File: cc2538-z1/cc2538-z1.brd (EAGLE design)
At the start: 56.8 x 34.5 mm, 101 parts, among them U1 CC2538, U10 DMG6602SVT, U2 CC1120_RHM_32, U3 TPD2E001IDRLRQ1, U4 CP2103, U5 BSS138PS, U6 BSS138PS, U7 BSS138PS, U8 M25P16VMN6P, U9 DMG6602SVT, X1 FA-128, X2 32MHz, X3 32.768K

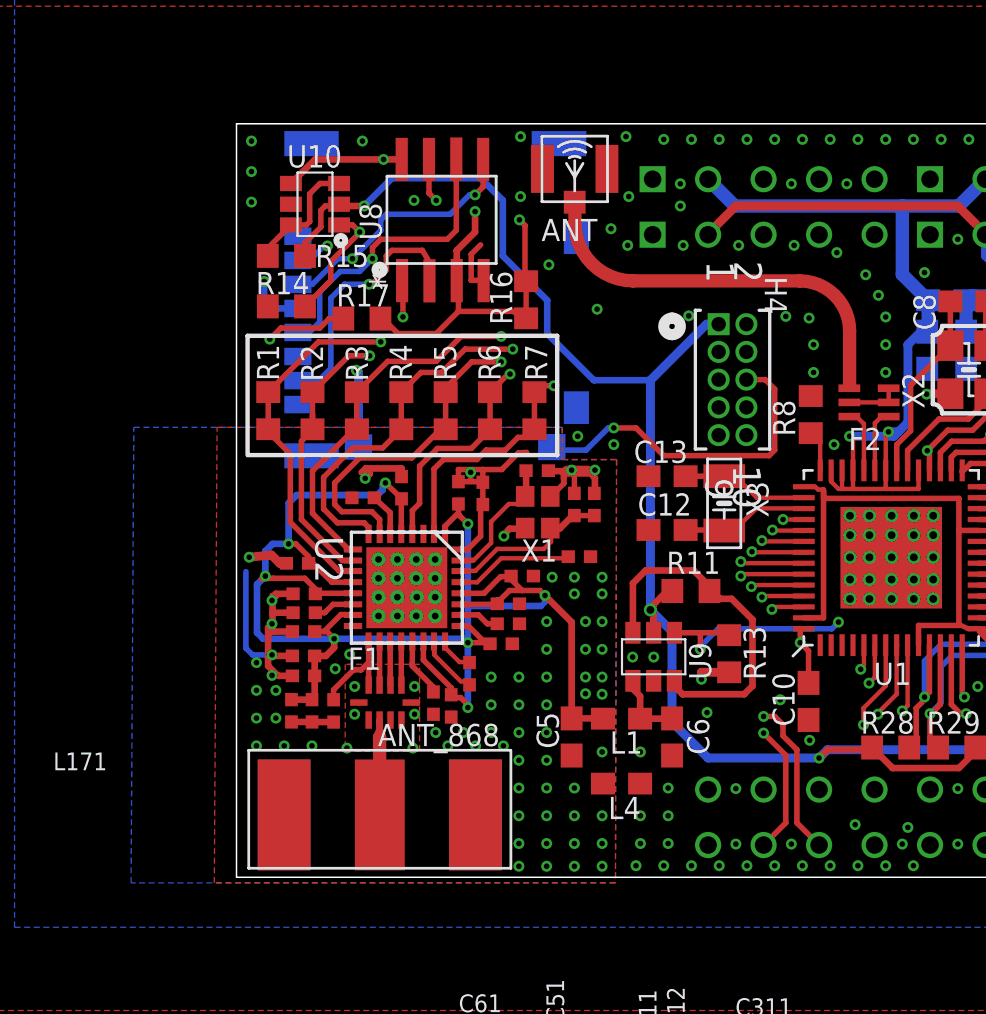
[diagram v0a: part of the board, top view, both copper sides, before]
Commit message: Added level translator for SPI power down, resized some DNP resistors, some other minor changes.
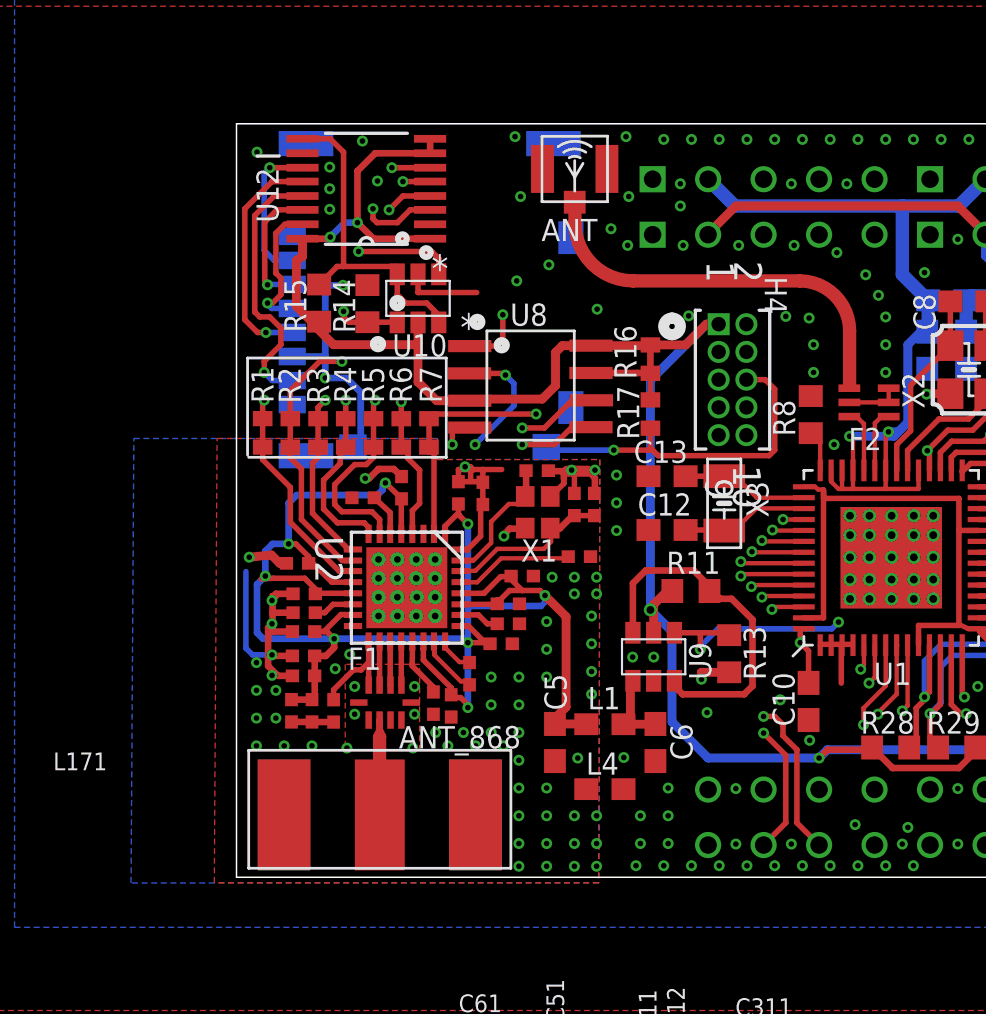
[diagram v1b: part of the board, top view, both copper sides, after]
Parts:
- added U12: SN74AVC4T774PW, CC11x:SOP65P640X120-16N
- R1, R2, R3, R4, R5, R6, R7: value (none) -> DNP; device rcl:R0603 -> rcl:R0402
- R16, R17: device rcl:R0603 -> rcl:R0402
- moved R17 13.9 mm to (18.9, 21.2), turned to 270 degrees
- moved U8 9.13 mm to (13.8, 22.5), turned to 0 degrees
- moved R16 6.31 mm to (18.9, 23.7), turned to 270 degrees
- moved R7 4.93 mm to (8.81, 20.3)
- moved U10 4.69 mm to (6.96, 27.3), turned to 0 degrees
- moved R6 4.19 mm to (7.54, 20.3)
- moved R14 3.71 mm to (5.99, 26.3), turned to 270 degrees
- moved R5 3.45 mm to (6.27, 20.3)
- moved R4 2.74 mm to (5.00, 20.3)
- moved R15 2.63 mm to (3.78, 26.3), turned to 270 degrees
- moved R3 2.05 mm to (3.73, 20.3)
- moved R2 1.44 mm to (2.46, 20.3)
- moved R1 1.05 mm to (1.20, 20.3)
- moved L1 0.80 mm to (16.9, 7.01)
- moved L4 0.80 mm to (16.9, 4.04)
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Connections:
- removed net N$43: R15.1, U10.P$3, U10.P$6
- removed net N$65: U1.4
- removed net N$66: U1.3
- removed net N$67: U1.2
- removed net N$68: U1.1
- new net N$42: R15.1, U10.P$3, U10.P$6, U12.9
- new net SD_BUF_CLK: SD1.5, U12.12
- new net SD_BUF_CSN: SD1.2, U12.11
- new net SD_BUF_MISO: SD1.7, U12.13
- new net SD_BUF_MOSI: SD1.3, U12.14
- net +3V3: now also R16.1, R16.2, R17.1, U12.1, U12.16, U12.7, U12.8, U8.3, U8.7, U8.8
- net GND: now also U1.1, U1.2, U1.3, U1.4, U12.10, U12.2
- net MEM_VCC: now also U12.15; no longer R16.1, R16.2, R17.1, U8.3, U8.7, U8.8
- net SD_SPI_CLK: now also U12.5; no longer SD1.5
- net SD_SPI_CSN: now also U12.6; no longer SD1.2
- net SD_SPI_MISO: now also U12.4; no longer SD1.7
- net SD_SPI_MOSI: now also U12.3; no longer SD1.3
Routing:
- net MEM_VCC: track 49.3 -> 16.8 mm, vias 5 -> 2
- net +3V3: track 195.7 -> 219.3 mm, vias 6 -> 7
- net JTAG_TDO/SD_PRESENCE: track 48.6 -> 27.0 mm, vias 3 -> 2
- net N$42: track 0.00 -> 15.9 mm
- net GND: track 87.4 -> 101.7 mm, vias 182 -> 187
- net SD_BUF_MISO: track 0.00 -> 12.3 mm, vias 0 -> 1
- net SD_BUF_CLK: track 0.00 -> 10.7 mm, vias 0 -> 1
- net SD_BUF_CSN: track 0.00 -> 6.86 mm, vias 0 -> 1
- net SD_BUF_MOSI: track 0.00 -> 6.24 mm, vias 0 -> 1
- net N$43: track 5.59 -> 0.00 mm
- net SD_SPI_CLK: track 61.3 -> 55.8 mm, vias 3 -> 4
- net JTAG_TDI/FLASH_SPI_CSN: track 57.8 -> 54.5 mm, vias 3 -> 2
- net RGND: track 36.1 -> 34.5 mm, vias 73 -> 65
- net SD_SPI_MOSI: track 63.1 -> 61.7 mm
- net RADIO_GPIO2: track 53.3 -> 54.7 mm
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
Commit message: Finalised board design?
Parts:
- added C20, C22: 1uF, CC11x:C0603
- added C23: 100nF, CC11x:C0603
- added U11: SN74AVC4T774PW, CC11x:SOP65P640X120-16N
- R10: value (none) -> 100k
- U12: value SN74AVC4T774PW -> TMP102AIDRLT; device CC11x:SOP65P640X120-16N -> CC11x:SOT50P160X60-6N
- moved U12 32.2 mm to (19.3, 2.26), turned to 270 degrees
- moved R10 28.1 mm to (11.2, 28.7), turned to 90 degrees
- moved ANT 0.76 mm to (14.7, 32.4)
- moved R13 0.25 mm to (22.3, 10.2)
- moved U8 0.08 mm to (13.9, 22.5)
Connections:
- removed net N$20: J1.4, R10.2
- removed net N$40: H1.C41
- removed net N$64: H1.B25
- new net TEMP_ALERT: H1.C41, U12.3
- net +3V3: now also C22.2, C23.2, U11.1, U11.16, U11.7, U11.8; no longer U12.1, U12.16, U12.7, U12.8
- net GND: now also C20.2, C22.1, C23.1, U11.10, U11.2, U12.4, U6.1, U6.2, U6.6; no longer U12.10
- net GNDA: no longer R10.1
- net I2C_SCL: now also U12.1
- net I2C_SDA: now also U12.6
- net JTAG_TDO/SD_PRESENCE: now also C20.1, R10.1
- net MEM_VCC: now also R10.2, U11.15; no longer U12.15
- net N$42: now also U11.9; no longer U12.9
- net PWR_SENSE_EN: now also H1.B25, U12.5
- net SD_BUF_CLK: now also U11.12; no longer U12.12
- net SD_BUF_CSN: now also U11.11; no longer U12.11
- net SD_BUF_MISO: now also U11.13; no longer U12.13
- net SD_BUF_MOSI: now also U11.14; no longer U12.14
- net SD_SPI_CLK: now also U11.5; no longer U12.5
- net SD_SPI_CSN: now also U11.6; no longer U12.6
- net SD_SPI_MISO: now also U11.4; no longer U12.4
- net SD_SPI_MOSI: now also U11.3; no longer U12.3
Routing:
- net GND: track 101.7 -> 168.5 mm, vias 187 -> 194
- net PWR_SENSE_EN: track 24.8 -> 81.4 mm, vias 1 -> 2
- net JTAG_TDI/FLASH_SPI_CSN: track 54.5 -> 31.2 mm
- net TEMP_ALERT: track 0.00 -> 21.3 mm, vias 0 -> 1
- net JTAG_TDO/SD_PRESENCE: track 27.0 -> 47.5 mm, vias 2 -> 4
- net I2C_SDA: track 37.5 -> 57.3 mm, vias 1 -> 3
- net I2C_SCL: track 37.4 -> 51.8 mm, vias 1 -> 3
- net MEM_VCC: track 16.8 -> 24.7 mm, vias 2 -> 3
- net N$20: track 6.33 -> 0.00 mm
- net GNDA: track 32.1 -> 28.3 mm
- net +3V3: track 219.3 -> 217.0 mm
- net PWR_RADIO_EN: track 48.2 -> 46.0 mm, vias 3 -> 2
- net SD_SPI_MISO: track 60.4 -> 59.3 mm
- net RADIO_GPIO2: track 54.7 -> 53.6 mm
- net DCOUPL: track 26.9 -> 27.8 mm
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- added copper zone on layer 1, net GNDA
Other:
- board text added: "1.0"
- board text added: "2.4G"
- board text added: "868MHz"
- board text added: "ANT"
- board text added: "April 2016"
- board text added: "ECS"
- board text added: "Graeme Bragg"
- board text added: "Muntjac"
- board text added: "Phil Basford"
- board text added: "University of Southampton"
